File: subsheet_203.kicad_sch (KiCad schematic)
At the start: 14 parts, among them U203 MC68901_DIP_48_PHY, U209 74LS86_PHY, U211 74LS04_PHY, U900 74LS164_PHY, Y200 2.4576 MHz

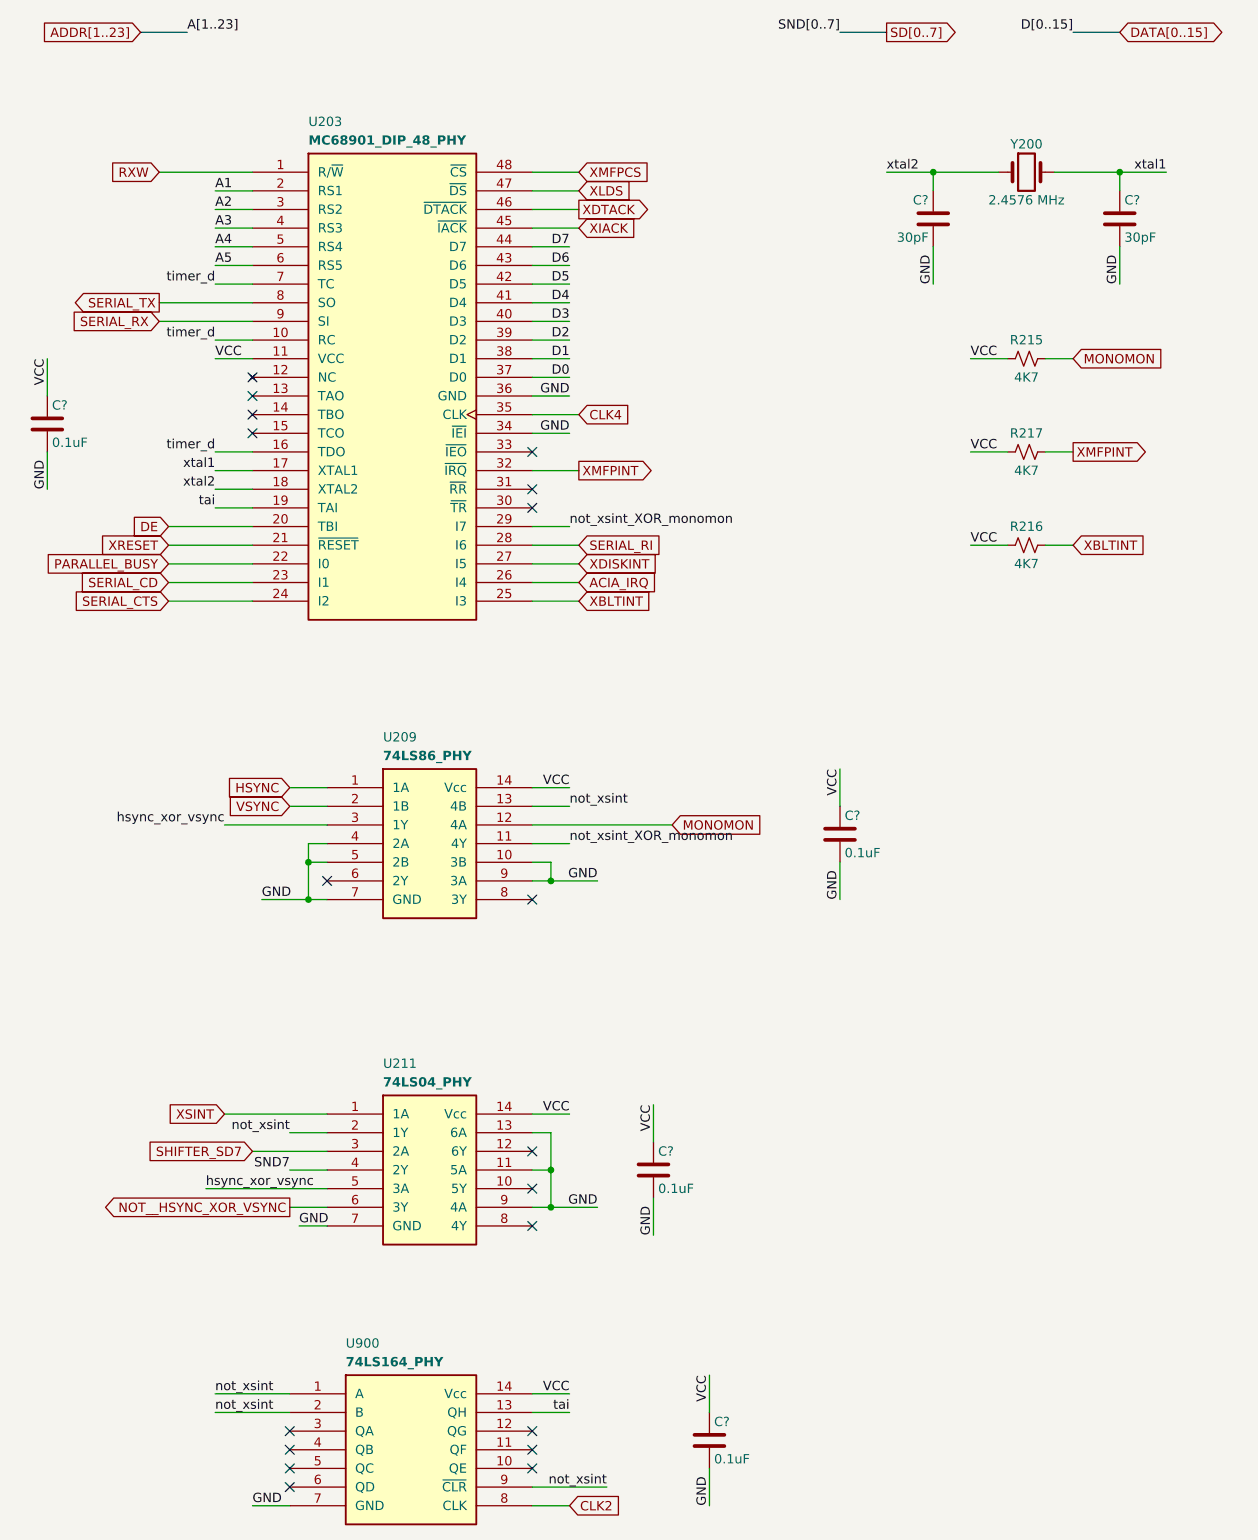
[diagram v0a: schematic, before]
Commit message: Resolves #3 : [schematic] annotate video port with signal name
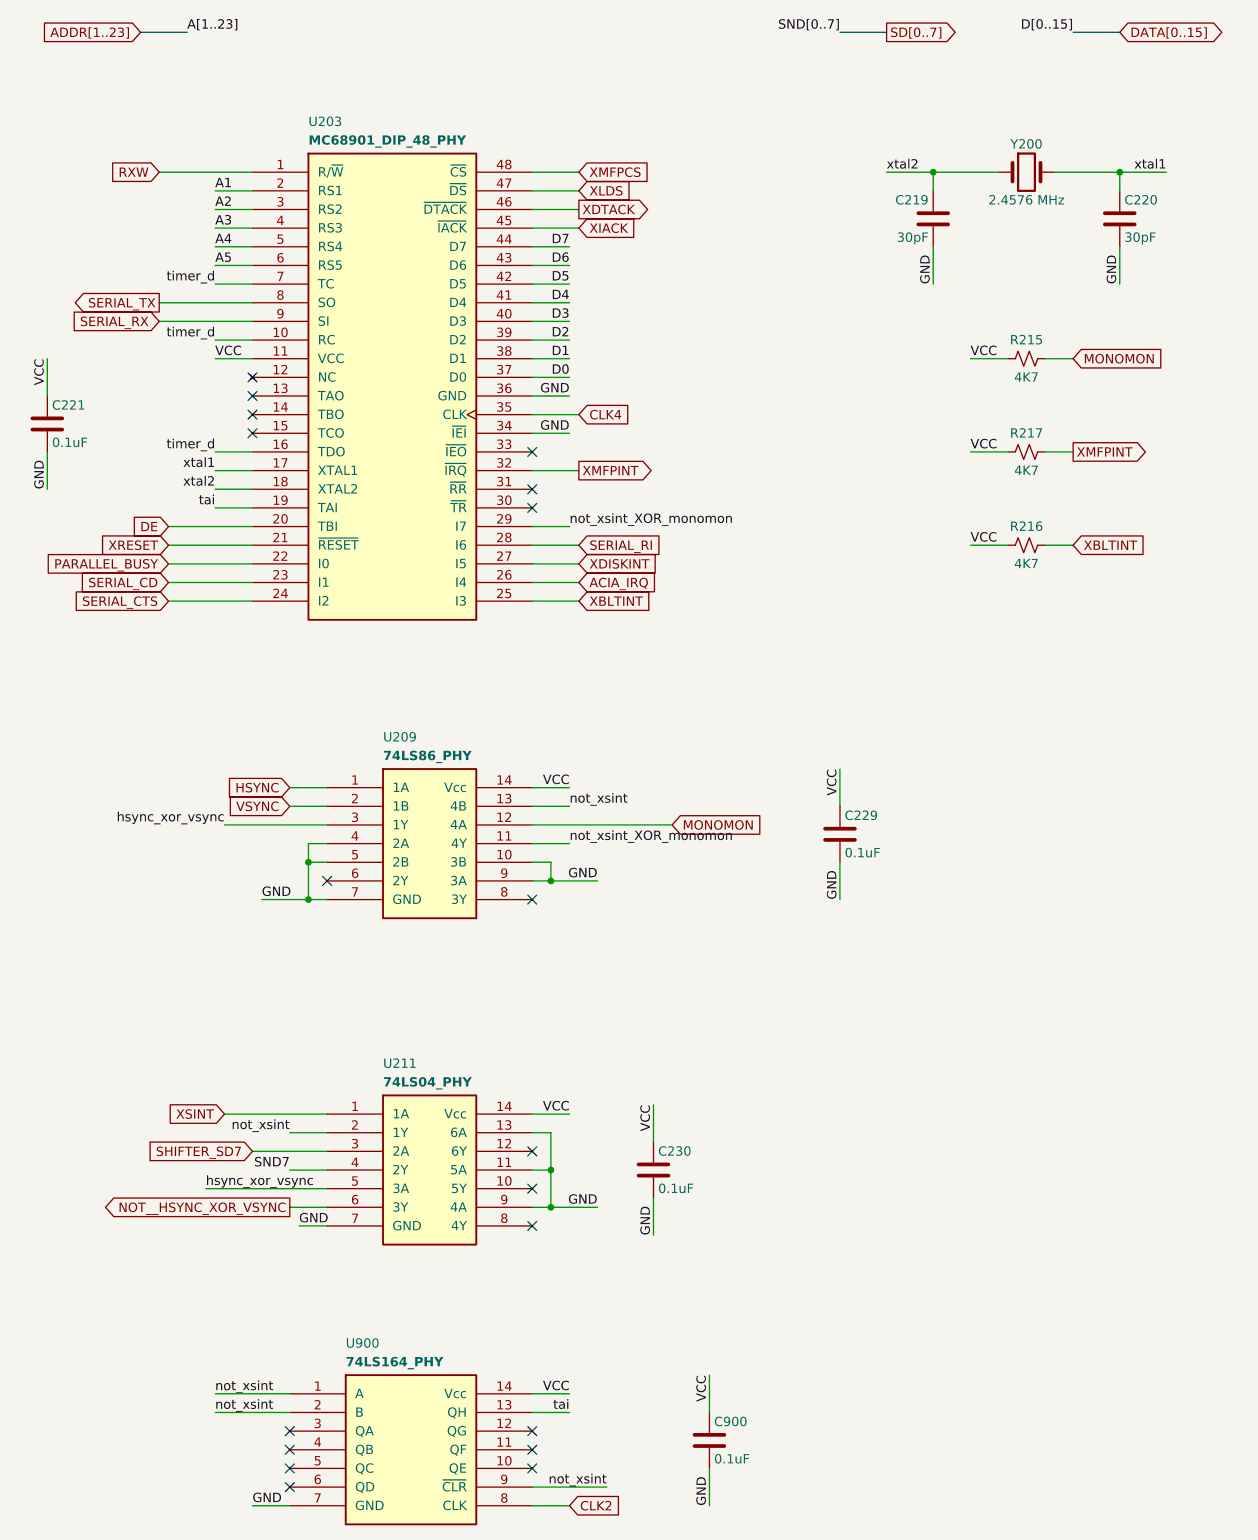
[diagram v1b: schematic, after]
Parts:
- gave numbers to parts that had none: 6
